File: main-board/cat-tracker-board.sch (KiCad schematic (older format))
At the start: 34 parts, among them J1 Conn_01x10, J2 USB C, Q1 CSD16301Q2, Q2 CSD16301Q2, SW1 PCM12SMTR, U1 ATSAMD21E18A-A, U2 BQ29737DSER, U3 L80-R, U4 RFM95W-915S2, U5 MCP73831-2ACI/MC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

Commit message: Change usb to micro B type.
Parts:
- removed J2: USB C, Connector_USB:USB_C_Receptacle_Amphenol_12401610E4-2A, symbol Connector:USB_C_Receptacle_USB2.0
- removed R10, R9: 5.1k, Resistor_SMD:R_0805_2012Metric, symbol Device:R
- added J3: USB_B_Micro, Connector_USB:USB_Micro-B_Amphenol_10103594-0001LF_Horizontal, symbol Connector:USB_B_Micro
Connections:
- wire segments 128 -> 122
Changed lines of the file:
@@
 Wire Wire Line
 	2850 3800 2850 4250
-$Comp
-L Connector:USB_C_Receptacle_USB2.0 J2
-U 1 1 60913954
-P 6750 1900
-F 0 "J2" H 6320 1839 50  0000 R CNN
-F 1 "USB C" H 6320 1748 50  0000 R CNN
-F 2 "Connector_USB:USB_C_Receptacle_Amphenol_12401610E4-2A" H 6900 1900 50  0001 C CNN
-F 3 "https://www.usb.org/sites/default/files/documents/usb_type-c.zip" H 6900 1900 50  0001 C CNN
-F 4 "Amphenol" H 6750 1900 50  0001 C CNN "mfg1"
-F 5 "12401610E4#2A" H 6750 1900 50  0001 C CNN "mfg1pn"
-	1    6750 1900
-	1    0    0    -1
-$EndComp
-Wire Wire Line
-	6750 2850 6750 2800
-Wire Wire Line
-	6450 2850 6450 2800
-Text HLabel 6450 2850 3    50   Input ~ 0
-GND
-Text HLabel 6750 2850 3    50   Input ~ 0
-GND
-Wire Wire Line
-	7400 1800 7350 1800
-Wire Wire Line
-	7400 2000 7350 2000
-Text HLabel 7400 1800 2    50   Input ~ 0
+Wire Wire Line
+	6800 2400 6800 2350
+Wire Wire Line
+	6700 2400 6700 2350
+Text HLabel 6700 2400 3    50   Input ~ 0
+GND
+Text HLabel 6800 2400 3    50   Input ~ 0
+GND
+Wire Wire Line
+	7150 2050 7100 2050
+Wire Wire Line
+	7150 1950 7100 1950
+Text HLabel 7150 2050 2    50   Input ~ 0
 USBDM
-Text HLabel 7400 2000 2    50   Input ~ 0
+Text HLabel 7150 1950 2    50   Input ~ 0
 USBDP
 Wire Wire Line
-	7400 2100 7350 2100
-Text HLabel 7400 2100 2    50   Input ~ 0
-USBDP
-Wire Wire Line
-	7400 1900 7350 1900
-Text HLabel 7400 1900 2    50   Input ~ 0
-USBDM
-$Comp
-L Device:R R9
-U 1 1 6091DC73
-P 7750 1500
-F 0 "R9" V 7543 1500 50  0000 C CNN
-F 1 "5.1k" V 7634 1500 50  0000 C CNN
-F 2 "Resistor_SMD:R_0805_2012Metric" V 7680 1500 50  0001 C CNN
-F 3 "~" H 7750 1500 50  0001 C CNN
-F 4 "Yageo" H 7750 1500 50  0001 C CNN "mfg1"
-F 5 "RC0805JR-075K1L" H 7750 1500 50  0001 C CNN "mfg1pn"
-	1    7750 1500
-	0    -1   1    0
-$EndComp
-Wire Wire Line
-	7900 1500 7950 1500
-Text HLabel 7950 1500 2    50   Input ~ 0
-GND
-$Comp
-L Device:R R10
-U 1 1 60920F65
-P 7750 1600
-F 0 "R10" V 7543 1600 50  0001 C CNN
-F 1 "5.1k" V 7634 1600 50  0001 C CNN
-F 2 "Resistor_SMD:R_0805_2012Metric" V 7680 1600 50  0001 C CNN
-F 3 "~" H 7750 1600 50  0001 C CNN
-F 4 "Yageo" H 7750 1600 50  0001 C CNN "mfg1"
-F 5 "RC0805JR-075K1L" H 7750 1600 50  0001 C CNN "mfg1pn"
-	1    7750 1600
-	0    -1   1    0
-$EndComp
-Wire Wire Line
-	7900 1600 7950 1600
-Text HLabel 7950 1600 2    50   Input ~ 0
-GND
-Wire Wire Line
-	7400 1300 7350 1300
-Text HLabel 7400 1300 2    50   Input ~ 0
+	7150 1750 7100 1750
+Text HLabel 7150 1750 2    50   Input ~ 0
 VUSB
-Wire Wire Line
-	7600 1500 7350 1500
-Wire Wire Line
-	7600 1600 7350 1600
 Wire Wire Line
 	1800 6300 1850 6300
@@
 Text Notes 12150 1450 0    50   ~ 0
 LoRa
+$Comp
+L Connector:USB_B_Micro J3
+U 1 1 60E667A5
+P 6800 1950
+F 0 "J3" H 6857 2417 50  0000 C CNN
+F 1 "USB_B_Micro" H 6857 2326 50  0000 C CNN
+F 2 "Connector_USB:USB_Micro-B_Amphenol_10103594-0001LF_Horizontal" H 6950 1900 50  0001 C CNN
+F 3 "~" H 6950 1900 50  0001 C CNN
+	1    6800 1950
+	1    0    0    -1
+$EndComp
 $EndSCHEMATC

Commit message: Change passives to 0603, change mcu to qfp, change battery to asr00007.
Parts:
- removed C8: 0.1 uF, Capacitor_SMD:C_0805_2012Metric, symbol Device:C
- removed Q1, Q2: CSD16301Q2, Package_SON:Texas_DQK, symbol Transistor_FET:CSD16301Q2
- removed R3: 2.2K, Resistor_SMD:R_0805_2012Metric, symbol Device:R
- removed R4: 330, Resistor_SMD:R_0805_2012Metric, symbol Device:R
- removed U1: ATSAMD21E18A-A, Package_QFP:TQFP-32_7x7mm_P0.8mm, symbol cat-tracker-board-rescue:ATSAMD21E18A-A-MCU_Microchip_SAMD
- removed U2: BQ29737DSER, Package_SON:WSON-6_1.5x1.5mm_P0.5mm, symbol Battery_Management:BQ297xy
- added U1: ATSAMD21E18A-M, Package_DFN_QFN:QFN-32-1EP_5x5mm_P0.5mm_EP3.6x3.6mm, symbol MCU_Microchip_SAMD:ATSAMD21E18A-M
- BT1: value Lir2477 -> ASR00007; footprint colinholzman:Keystone_3039 -> colinholzman:TinyCircuits_ASR00007; description (none) -> 23x25x5.5 mm, 290 mAh, li-ion; mfg1 Keystone -> TinyCircuits; mfg1pn 3039 -> ASR00007
- C1, C10, C9: footprint Capacitor_SMD:C_0805_2012Metric -> Capacitor_SMD:C_0603_1608Metric; description (none) -> MLCC, 1 uF, 16 V, X7R, 0603; mfg1 Wurth Elektronik -> TDK; mfg1pn 885012207051 -> CGA3E1X7R1C105K080AC
- C2, C4: footprint Capacitor_SMD:C_0805_2012Metric -> Capacitor_SMD:C_0603_1608Metric; description (none) -> MLCC, 10 uF, 16 V, X5R, 0603; mfg1pn EMK212BB7106MG-T -> EMK107BBJ106MA-T
- C3, C5: footprint Capacitor_SMD:C_0805_2012Metric -> Capacitor_SMD:C_0603_1608Metric; description (none) -> MLCC, 0.1 uF, 16 V, X7R, 0603; mfg1 AVX -> KEMET; mfg1pn 08055C104KAT2A -> C0603C104M4RAC7411
- C6, C7: footprint Capacitor_SMD:C_0805_2012Metric -> Capacitor_SMD:C_0603_1608Metric; description (none) -> MLCC, 4.7 uF, 16 V, X5R, 0603; mfg1 Murata Electronics -> TDK; mfg1pn GRM21BR71C475KE51L -> C1608X5R1C475K080AE
- D1: value SMAJ5.0A -> PTVS5V0S1UTR,115; footprint Diode_SMD:D_SMA -> Diode_SMD:D_SOD-123; description (none) -> TVS, 5 V, 400 W, SOD-123; mfg1 Vishay -> Nexperia; mfg1pn SMAJ5.0A-E3/61 -> PTVS5V0S1UTR,115
- D2: footprint LED_SMD:LED_0805_2012Metric -> LED_SMD:LED_0603_1608Metric; description (none) -> LED, red, 0603; mfg1 Lite-On -> Wurth Elektronik; mfg1pn LTST-C171KRKT -> 150060RS75000
- D4: description (none) -> TVS, dual, 5.5 V, SOT-143B-4
- FB1: footprint Inductor_SMD:L_0805_2012Metric -> Inductor_SMD:L_0603_1608Metric; description (none) -> Ferrite Bead, 150 Ohm, 750 mA, 0603; mfg1pn BLM21AG151SN1D -> BLM18AG151SN1D
- J3: mfg1 (none) -> Amphenol; mfg1pn (none) -> 10103594-0001LF
- R1, R2: footprint Resistor_SMD:R_0805_2012Metric -> Resistor_SMD:R_0603_1608Metric; description (none) -> Resistor, 100 kOhm, 0603; mfg1 Vishay / Dale -> Panasonic; mfg1pn CRCW0805100KJNEAC -> ERJ-3EKF1003V
- R5: footprint Resistor_SMD:R_0805_2012Metric -> Resistor_SMD:R_0603_1608Metric; description (none) -> Resistor, 750 Ohm, 0603; mfg1 Panasonic -> Yageo; mfg1pn ERJ-6GEYJ751V -> AC0603JR-07750RL
- R6: footprint Resistor_SMD:R_0805_2012Metric -> Resistor_SMD:R_0603_1608Metric; description (none) -> Resistor, 14 kOhm, 0603; mfg1 Bourns -> Yageo; mfg1pn CR0805-FX-1402ELF -> RC0603FR-0714KL
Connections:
- net labels added: RX, TX
- wire segments 122 -> 104
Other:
- moved on the sheet: BT1

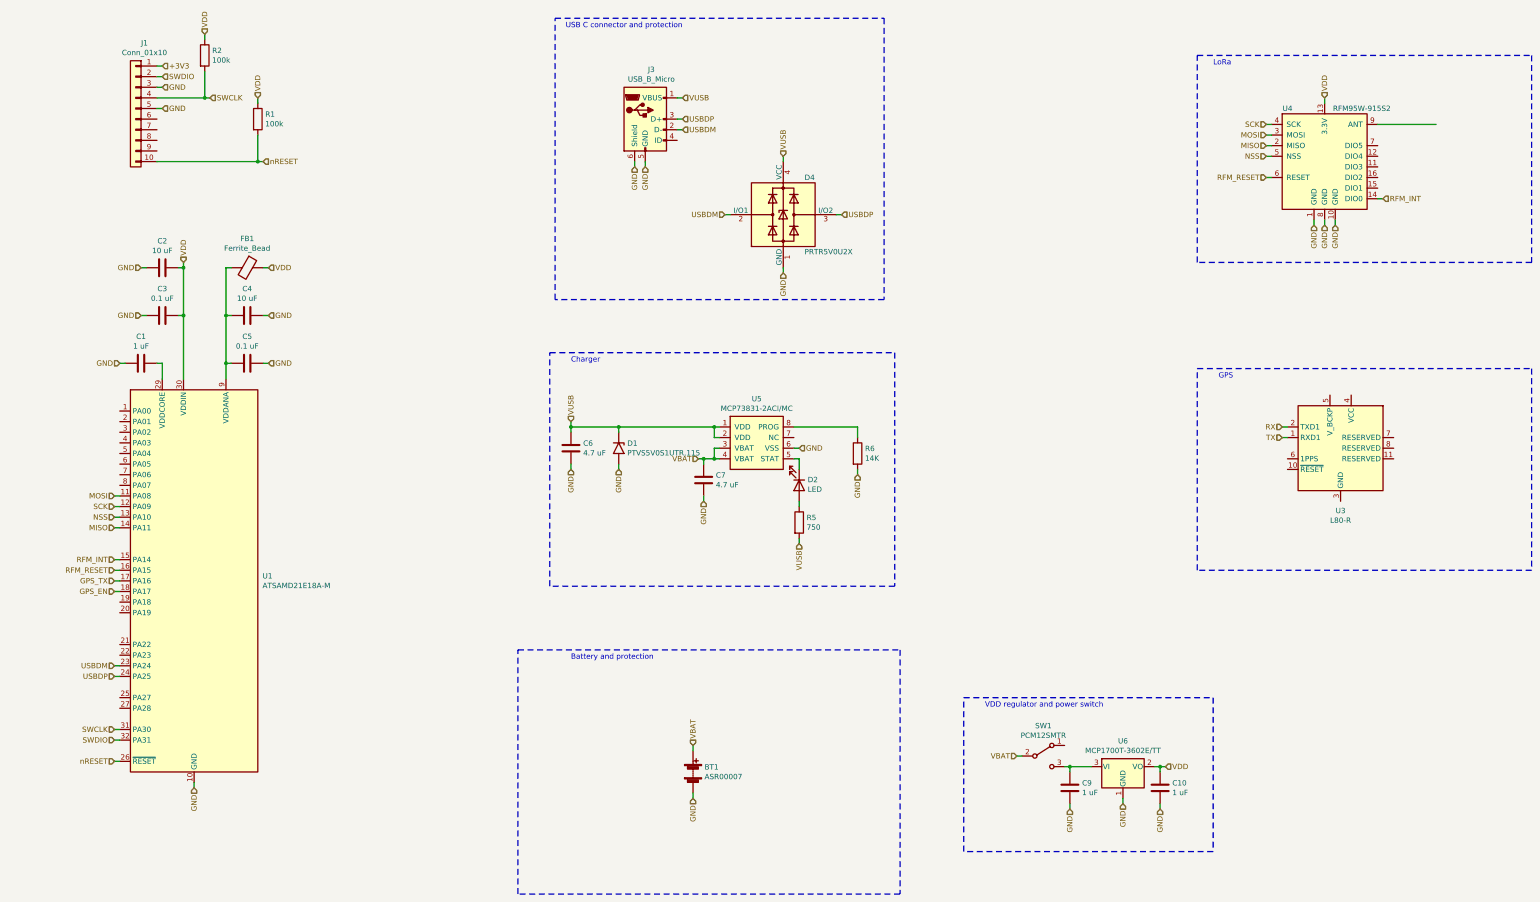
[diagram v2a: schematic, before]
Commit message: Add antenna, change USB to smd, add gps switch, connect gps.
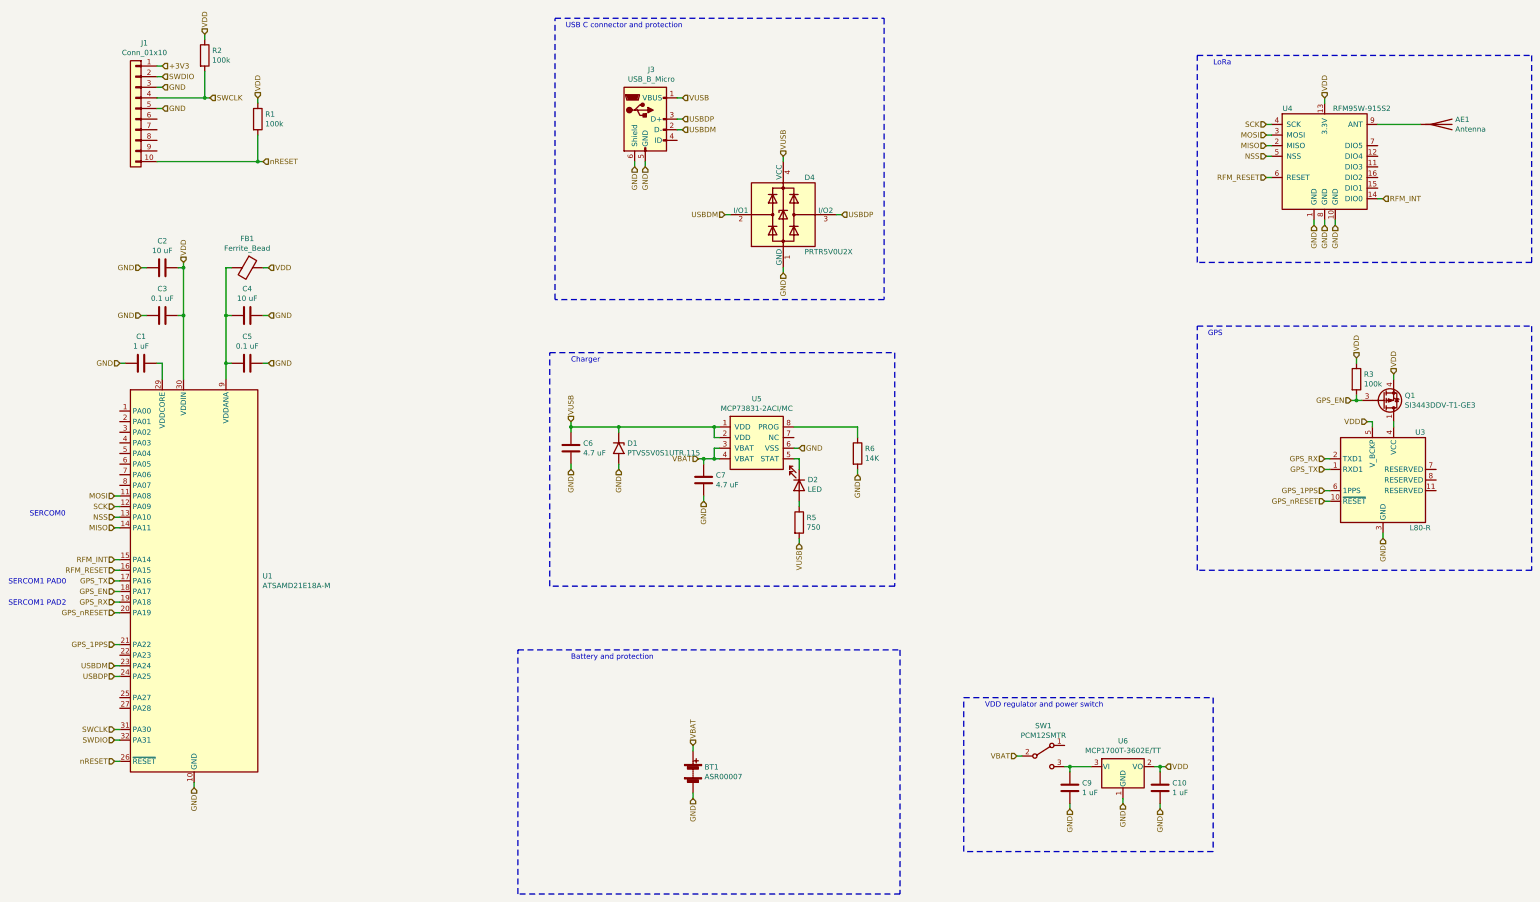
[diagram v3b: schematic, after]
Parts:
- added AE1: Antenna, RF_Antenna:Texas_SWRA416_868MHz_915MHz, symbol Device:Antenna
- added Q1: SI3443DDV-T1-GE3, Package_SO:TSOP-6_1.65x3.05mm_P0.95mm, symbol colinholzman:Si3443
- added R3: 100k, Resistor_SMD:R_0603_1608Metric, symbol Device:R
- J3: footprint Connector_USB:USB_Micro-B_Amphenol_10103594-0001LF_Horizontal -> colinholzman:USB_Micro-B_Amphenol_10118192_Horizontal; mfg1pn 10103594-0001LF -> 10118192-0001LF
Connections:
- net RX is gone; now on net GPS_RX: U3.2 (TXD1)
- net TX is gone; now on net GPS_TX: U3.1 (RXD1)
- net GND: now also U3.12 (GND), U3.3 (GND)
- net GPS_EN: now also Q1.3 (G), R3.2
- net VDD: now also U3.5 (V_BCKP), Q1.4 (S), R3.1
- net at U4.9 (ANT): now also AE1.1 (A)
- net GPS_nRESET: now reaches U3.10 (~RESET)
- net GPS_nRESET: now also U1.20 (PA19)
- net at U3.4 (VCC): now also Q1.1 (D), Q1.2 (D), Q1.5 (D), Q1.6 (D)
- net GPS_1PPS: now reaches U3.6 (1PPS)
- net GPS_1PPS: now also U1.21 (PA22)
- net GPS_RX: now reaches U1.19 (PA18)
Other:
- note added: "SERCOM0"
- note added: "SERCOM1 PAD0"
- note added: "SERCOM1 PAD2"
- moved on the sheet: U3
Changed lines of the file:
@@
 GPS_EN
 Wire Wire Line
-	13700 2000 14250 2000
+	13700 2000 14100 2000
 Wire Wire Line
 	8100 2300 8100 2350
@@
 L cat-tracker-board-rescue:L80-R-RF_GPS U3
 U 1 1 60E2275D
-P 13350 5050
-F 0 "U3" H 13350 4461 50  0000 C CNN
-F 1 "L80-R" H 13350 4370 50  0000 C CNN
-F 2 "RF_GPS:Quectel_L80-R" H 13350 4150 50  0001 C CNN
-F 3 "https://www.quectel.com/UploadImage/Downlad/Quectel_L80-R_Hardware_Design_V1.2.pdf" H 13350 5050 50  0001 C CNN
-F 4 "Quectel" H 13350 5050 50  0001 C CNN "mfg1"
-F 5 "L80RE-M37" H 13350 5050 50  0001 C CNN "mfg1pn"
-	1    13350 5050
+P 13750 5350
+F 0 "U3" H 13400 5800 50  0000 C CNN
+F 1 "L80-R" H 13400 4900 50  0000 C CNN
+F 2 "RF_GPS:Quectel_L80-R" H 13750 4450 50  0001 C CNN
+F 3 "https://www.quectel.com/UploadImage/Downlad/Quectel_L80-R_Hardware_Design_V1.2.pdf" H 13750 5350 50  0001 C CNN
+F 4 "Quectel" H 13750 5350 50  0001 C CNN "mfg1"
+F 5 "L80RE-M37" H 13750 5350 50  0001 C CNN "mfg1pn"
+	1    13750 5350
 	-1   0    0    -1
 $EndComp
@@
 	12000 3300 12000 1350
 Wire Notes Line
-	15150 4300 15150 6200
+	15150 3900 15150 6200
 Wire Notes Line
 	15150 6200 12000 6200
 Wire Notes Line
-	12000 6200 12000 4300
-Wire Notes Line
-	12000 4300 15150 4300
-Text Notes 12200 4400 0    50   ~ 0
+	12000 6200 12000 3900
+Wire Notes Line
+	12000 3900 15150 3900
+Text Notes 12100 4000 0    50   ~ 0
 GPS
 Text Notes 12150 1450 0    50   ~ 0
@@
 F 0 "J3" H 6857 2417 50  0000 C CNN
 F 1 "USB_B_Micro" H 6857 2326 50  0000 C CNN
-F 2 "Connector_USB:USB_Micro-B_Amphenol_10103594-0001LF_Horizontal" H 6950 1900 50  0001 C CNN
+F 2 "colinholzman:USB_Micro-B_Amphenol_10118192_Horizontal" H 6950 1900 50  0001 C CNN
 F 3 "~" H 6950 1900 50  0001 C CNN
 F 4 "Amphenol" H 6800 1950 50  0001 C CNN "mfg1"
-F 5 "10103594-0001LF" H 6800 1950 50  0001 C CNN "mfg1pn"
+F 5 "10118192-0001LF" H 6800 1950 50  0001 C CNN "mfg1pn"
 	1    6800 1950
 	1    0    0    -1
@@
 	1    0    0    -1
 $EndComp
-Wire Wire Line
-	12800 4850 12850 4850
-Wire Wire Line
-	12800 4950 12850 4950
-Text HLabel 12800 4850 0    50   Input ~ 0
-RX
-Text HLabel 12800 4950 0    50   Input ~ 0
-TX
+$Comp
+L colinholzman:Si3443 Q1
+U 1 1 60E6BE86
+P 13750 4600
+F 0 "Q1" H 13955 4554 50  0000 L CNN
+F 1 "SI3443DDV-T1-GE3" H 13955 4645 50  0000 L CNN
+F 2 "Package_SO:TSOP-6_1.65x3.05mm_P0.95mm" H 13950 4700 50  0001 C CNN
+F 3 "~" H 13750 4600 50  0001 C CNN
+F 4 "Vishay Semiconductors" H 13750 4600 50  0001 C CNN "mfg1"
+F 5 "SI3443DDV-T1-GE3" H 13750 4600 50  0001 C CNN "mfg1pn"
+	1    13750 4600
+	1    0    0    1
+$EndComp
+Wire Wire Line
+	13850 4850 13850 4800
+Wire Wire Line
+	13850 4350 13850 4400
+Text HLabel 13850 4350 1    50   Input ~ 0
+VDD
+$Comp
+L Device:R R3
+U 1 1 60EADECE
+P 13500 4400
+F 0 "R3" H 13570 4446 50  0000 L CNN
+F 1 "100k" H 13570 4355 50  0000 L CNN
+F 2 "Resistor_SMD:R_0603_1608Metric" V 13430 4400 50  0001 C CNN
+F 3 "~" H 13500 4400 50  0001 C CNN
+F 4 "Panasonic" H 13500 4400 50  0001 C CNN "mfg1"
+F 5 "ERJ-3EKF1003V" H 13500 4400 50  0001 C CNN "mfg1pn"
+F 6 "Resistor, 100 kOhm, 0603" H 13500 4400 50  0001 C CNN "description"
+	1    13500 4400
+	1    0    0    -1
+$EndComp
+Wire Wire Line
+	13500 4600 13500 4550
+Wire Wire Line
+	13550 4600 13500 4600
+Wire Wire Line
+	13500 4200 13500 4250
+Text HLabel 13500 4200 1    50   Input ~ 0
+VDD
+Wire Wire Line
+	13450 4600 13500 4600
+Connection ~ 13500 4600
+Text HLabel 13450 4600 0    50   Input ~ 0
+GPS_EN
+Wire Wire Line
+	13600 4800 13650 4800
+Text HLabel 13600 4800 0    50   Input ~ 0
+VDD
+Wire Wire Line
+	13650 4800 13650 4850
+Wire Wire Line
+	13750 5900 13750 5850
+Text HLabel 13750 5900 3    50   Input ~ 0
+GND
+Wire Wire Line
+	13200 5550 13250 5550
+Text HLabel 13200 5550 0    50   Input ~ 0
+GPS_nRESET
+Wire Wire Line
+	13200 5450 13250 5450
+Text HLabel 13200 5450 0    50   Input ~ 0
+GPS_1PPS
+Wire Wire Line
+	1800 6600 1850 6600
+Text HLabel 1800 6600 0    50   Input ~ 0
+GPS_nRESET
+Wire Wire Line
+	1800 6900 1850 6900
+Text HLabel 1800 6900 0    50   Input ~ 0
+GPS_1PPS
+Wire Wire Line
+	13200 5250 13250 5250
+Text HLabel 13200 5250 0    50   Input ~ 0
+GPS_TX
+Wire Wire Line
+	13200 5150 13250 5150
+Text HLabel 13200 5150 0    50   Input ~ 0
+GPS_RX
+Wire Wire Line
+	1800 6500 1850 6500
+Text HLabel 1800 6500 0    50   Input ~ 0
+GPS_RX
+Text Notes 800  6340 0    50   ~ 0
+SERCOM1 PAD0
+Text Notes 800  6540 0    50   ~ 0
+SERCOM1 PAD2
+Text Notes 1000 5700 0    50   ~ 0
+SERCOM0
+$Comp
+L Device:Antenna AE1
+U 1 1 60F07981
+P 14300 2000
+F 0 "AE1" V 14254 2130 50  0000 L CNN
+F 1 "Antenna" V 14345 2130 50  0000 L CNN
+F 2 "RF_Antenna:Texas_SWRA416_868MHz_915MHz" H 14300 2000 50  0001 C CNN
+F 3 "~" H 14300 2000 50  0001 C CNN
+	1    14300 2000
+	0    1    1    0
+$EndComp
 $EndSCHEMATC

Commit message: Rescue MCU symbol.
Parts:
- U1: symbol MCU_Microchip_SAMD:ATSAMD21E18A-M -> cat-tracker-board-rescue:ATSAMD21E18A-M-MCU_Microchip_SAMD
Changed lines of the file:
@@
 	7250 8350 7250 8300
 $Comp
-L MCU_Microchip_SAMD:ATSAMD21E18A-M U1
+L cat-tracker-board-rescue:ATSAMD21E18A-M-MCU_Microchip_SAMD U1
 U 1 1 60E817D0
 P 2550 6300

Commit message: Rearrange parts.
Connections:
- net USBDM renamed USBD-
- net USBDP renamed USBD+
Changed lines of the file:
@@
 Text HLabel 1800 8000 0    50   Input ~ 0
 nRESET
-Wire Wire Line
-	1800 7100 1850 7100
-Wire Wire Line
-	1800 7200 1850 7200
-Text HLabel 1800 7100 0    50   Input ~ 0
-USBDM
-Text HLabel 1800 7200 0    50   Input ~ 0
-USBDP
 $Comp
 L Device:C C2
@@
 	7150 1950 7100 1950
 Text HLabel 7150 2050 2    50   Input ~ 0
-USBDM
+USBD-
 Text HLabel 7150 1950 2    50   Input ~ 0
-USBDP
+USBD+
 Wire Wire Line
 	7150 1750 7100 1750
@@
 Text HLabel 8100 3400 3    50   Input ~ 0
 GND
-Wire Wire Line
-	8650 2850 8600 2850
-Text HLabel 8650 2850 2    50   Input ~ 0
-USBDP
-Wire Wire Line
-	7550 2850 7600 2850
 $Comp
 L Power_Protection:PRTR5V0U2X D4
@@
 Wire Wire Line
 	7450 4950 7500 4950
-Text HLabel 7550 2850 0    50   Input ~ 0
-USBDM
 Wire Wire Line
 	8200 5050 8250 5050
@@
 	0    1    1    0
 $EndComp
+Text HLabel 7550 2850 0    50   Input ~ 0
+USBD-
+Text HLabel 8650 2850 2    50   Input ~ 0
+USBD+
+Wire Wire Line
+	7550 2850 7600 2850
+Wire Wire Line
+	8600 2850 8650 2850
+Wire Wire Line
+	1800 7100 1850 7100
+Wire Wire Line
+	1800 7200 1850 7200
+Text HLabel 1800 7100 0    50   Input ~ 0
+USBD-
+Text HLabel 1800 7200 0    50   Input ~ 0
+USBD+
 $EndSCHEMATC

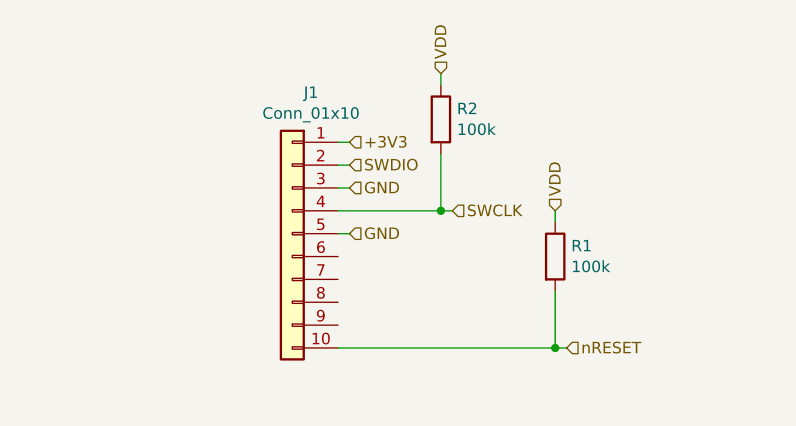
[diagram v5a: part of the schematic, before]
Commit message: Add some tracks.
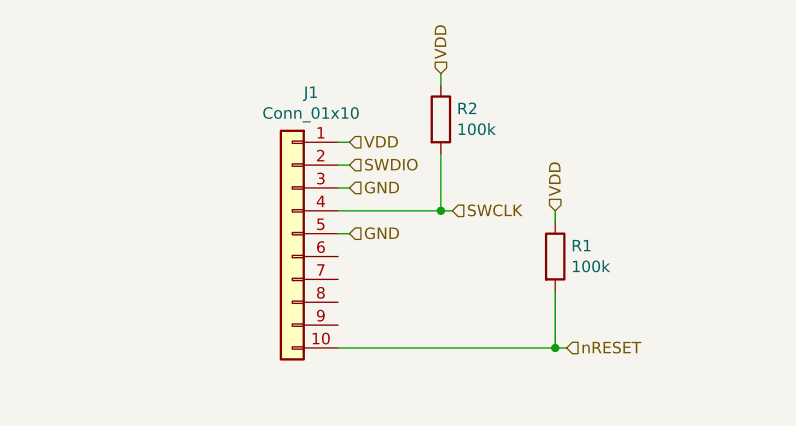
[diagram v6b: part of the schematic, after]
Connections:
- net +3V3 is gone; now on net VDD: J1.1 (Pin_1)
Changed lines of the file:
@@
 	2250 1450 2200 1450
 Text HLabel 2250 1450 2    50   Input ~ 0
-+3V3
+VDD
 Text HLabel 2250 1550 2    50   Input ~ 0
 SWDIO
